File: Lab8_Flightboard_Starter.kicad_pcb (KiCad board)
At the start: 2 copper layers, 80 x 80 mm, 64 parts, among them J1 Motor1, J10 ESC3_GND, J11 ESC4_VBAT, J12 ESC4_GND, J2 Motor2, J3 Motor3, J4 Motor4, J5 ESC1_VBAT, J6 ESC1_GND, J7 ESC2_VBAT, J8 ESC2_GND, J9 ESC3_VBAT, Q1 DMP6023LE-13, U1 Teensy4.0, U2 TPS62933, U4 LP5912-3.3DRV, U5 LP5912-3.3DRV, U6 NRF24L01_Breakout, U9 LSM6DSO32_Adafruit

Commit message: Added hole positions
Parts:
- moved H2 115.5 mm to (214.0, 73.5)
- moved H4 114.9 mm to (214.0, 98.5)
- moved H3 90.2 mm to (189.0, 98.5)
- moved H1 90.2 mm to (189.0, 73.5)
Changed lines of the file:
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@@
 	(footprint "FC_Mechanical:MountingHole_3.3mm_no-courtyard"
 		(layer "F.Cu")
-		(at 99.13 85.95)
+		(at 214 73.5)
 		(descr "Mounting Hole 3.3mm, no annular, no courtyard")
 		(tags "mounting hole 3.3mm no annular, no courtyard")
@@
 	(footprint "FC_Mechanical:MountingHole_3.3mm_no-courtyard"
 		(layer "F.Cu")
-		(at 99.13 94.55)
+		(at 214 98.5)
 		(descr "Mounting Hole 3.3mm, no annular, no courtyard")
 		(tags "mounting hole 3.3mm no annular, no courtyard")
@@
 	(footprint "FC_Mechanical:MountingHole_3.3mm_no-courtyard"
 		(layer "F.Cu")
-		(at 99.13 81.65)
+		(at 189 73.5)
 		(descr "Mounting Hole 3.3mm, no annular, no courtyard")
 		(tags "mounting hole 3.3mm no annular, no courtyard")
@@
 	(footprint "FC_Mechanical:MountingHole_3.3mm_no-courtyard"
 		(layer "F.Cu")
-		(at 99.13 90.25)
+		(at 189 98.5)
 		(descr "Mounting Hole 3.3mm, no annular, no courtyard")
 		(tags "mounting hole 3.3mm no annular, no courtyard")

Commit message: Added key component locations
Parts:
- moved J7 159.9 mm to (230.1, 50.6)
- moved J8 159.9 mm to (237.4, 50.6)
- moved U6 143.4 mm to (231.7, 91.4)
- moved J11 142.1 mm to (230.2, 122.0)
- moved J12 142.1 mm to (237.5, 122.0)
- moved U9 137.5 mm to (201.5, 60.6)
- moved U1 122.4 mm to (200.9, 95.4), turned to 90 degrees
- moved J5 108.4 mm to (173.0, 50.1), turned to 180 degrees
- moved J6 97.5 mm to (165.7, 50.1), turned to 180 degrees
- moved J9 84.6 mm to (173.1, 121.3), turned to 180 degrees
- moved BT1 75.8 mm to (166.5, 88.0), turned to -90 degrees
- moved J10 70.2 mm to (165.8, 121.3), turned to 180 degrees
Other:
- board size 80 x 80 mm -> 80.5 x 80.5 mm

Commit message: Added motor through holes
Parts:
- moved J2 172.3 mm to (223.0, 64.5), turned to 90 degrees
- moved J4 150.1 mm to (223.0, 110.0), turned to 90 degrees
- moved J1 139.0 mm to (181.0, 64.5), turned to -90 degrees
- moved J3 113.3 mm to (181.0, 110.0), turned to -90 degrees
- moved U6 7.11 mm to (233.0, 84.4)
- moved U1 0.74 mm to (201.6, 95.4)
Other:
- board size 80.5 x 80.5 mm -> 80 x 80 mm

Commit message: Edited F Silkscreen text
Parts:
- Teensy 4.0: renamed from U1
- moved L1 101.5 mm to (178.5, 102.0), turned to 180 degrees
- moved C6 70.0 mm to (171.5, 107.5), turned to 90 degrees
- moved D2 67.0 mm to (178.5, 95.0), turned to 180 degrees
- renumbered U9 to LSM, J1 to M1, J2 to M2, J3 to M3, J4 to M4, U6 to NRF
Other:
- board text added: "J10"
- board text added: "J11"
- board text added: "J12"
- board text added: "J7"
- board text added: "J8"
- board text added: "J9"

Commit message: Placed down more components
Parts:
- moved Q1 112.4 mm to (177.5, 79.0)
- moved D1 73.8 mm to (186.0, 88.0)
- moved C2 69.4 mm to (172.5, 97.5), turned to -90 degrees
- moved C6 4.24 mm to (174.5, 104.5)
- moved D2 3.50 mm to (182.0, 95.0)
- moved L1 3.00 mm to (181.5, 102.0)
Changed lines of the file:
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@@
 			(at 0 1.85 0)
 			(layer "F.Fab")
+			(hide yes)
 			(effects
 				(font
@@
 	(footprint "Capacitor_SMD:C_1206_3216Metric_Pad1.33x1.80mm_HandSolder"
 		(layer "F.Cu")
-		(at 104.285 84.525)
+		(at 172.5 97.5 -90)
 		(descr "Capacitor SMD 1206 (3216 Metric), square (rectangular) end terminal, IPC-7351 nominal with elongated pad for handsoldering. (Body size source: IPC-SM-782 page 76, https://www.pcb-3d.com/wordpress/wp-content/uploads/ipc-sm-782a_amendment_1_and_2.pdf)")
 		(tags "capacitor handsolder")
 		(property "Reference" "C2"
-			(at 0 -1.85 0)
+			(at 0 -1.85 90)
 			(layer "F.SilkS")
 			(effects
@@
 		)
 		(property "Value" "10u"
-			(at 0 1.85 0)
+			(at 0 1.85 90)
 			(layer "F.Fab")
+			(hide yes)
 			(effects
 				(font
@@
 		)
 		(property "Datasheet" ""
-			(at 0 0 0)
+			(at 0 0 90)
 			(layer "F.Fab")
 			(hide yes)
@@
 		)
 		(property "Description" "Unpolarized capacitor, small symbol"
-			(at 0 0 0)
+			(at 0 0 90)
 			(layer "F.Fab")
 			(hide yes)
@@
 		)
 		(property "KiLib_Generator" "SMD_2terminal_chip_molded"
-			(at 0 0 0)
+			(at 0 0 90)
 			(layer "F.SilkS")
 			(hide yes)
@@
 		(duplicate_pad_numbers_are_jumpers no)
 		(fp_line
-			(start -0.711252 -0.91)
-			(end 0.711252 -0.91)
+			(start -0.711252 0.91)
+			(end 0.711252 0.91)
 			(stroke
 				(width 0.12)
@@
 		)
 		(fp_line
-			(start -0.711252 0.91)
-			(end 0.711252 0.91)
+			(start -0.711252 -0.91)
+			(end 0.711252 -0.91)
 			(stroke
 				(width 0.12)
@@
 			(layer "F.Fab")
 		)
-		(fp_text user "${REFERENCE}"
-			(at 0 0 0)
-			(layer "F.Fab")
-			(effects
-				(font
-					(size 0.8 0.8)
-					(thickness 0.12)
-				)
-			)
-		)
 		(pad "1" smd roundrect
-			(at -1.5625 0)
+			(at -1.5625 0 270)
 			(size 1.325 1.8)
 			(layers "F.Cu" "F.Mask" "F.Paste")
@@
 		)
 		(pad "2" smd roundrect
-			(at 1.5625 0)
+			(at 1.5625 0 270)
 			(size 1.325 1.8)
 			(layers "F.Cu" "F.Mask" "F.Paste")
@@
 	(footprint "FC_Power_Footprints:SMBJSeries_LTF"
 		(layer "F.Cu")
-		(at 112.4382 82.2987)
+		(at 186 88)
 		(tags "SMBJ17A ")
 		(property "Reference" "D1"
-			(at 0 0 0)
+			(at 0 -2.7987 0)
 			(unlocked yes)
 			(layer "F.SilkS")
@@
 			(unlocked yes)
 			(layer "F.Fab")
+			(hide yes)
 			(effects
 				(font
@@
 			(layer "F.Fab")
 		)
-		(fp_text user "${REFERENCE}"
-			(at 0 0 0)
-			(unlocked yes)
-			(layer "F.Fab")
-			(effects
-				(font
-					(size 1 1)
-					(thickness 0.15)
-				)
-			)
-		)
 		(pad "1" smd rect
 			(at -1.8542 0 90)
@@
 			(polygon
 				(pts
-					(xy 109.695 80.381) (xy 115.1814 80.381) (xy 115.1814 81.1557) (xy 109.695 81.1557)
+					(xy 183.2568 86.0823) (xy 188.7432 86.0823) (xy 188.7432 86.857) (xy 183.2568 86.857)
 				)
 			)
@@
 			(polygon
 				(pts
-					(xy 109.695 83.4417) (xy 115.1814 83.4417) (xy 115.1814 84.2164) (xy 109.695 84.2164)
+					(xy 183.2568 89.143) (xy 188.7432 89.143) (xy 188.7432 89.9177) (xy 183.2568 89.9177)
 				)
 			)
@@
 			(polygon
 				(pts
-					(xy 111.727 81.1557) (xy 113.1494 81.1557) (xy 113.1494 83.4417) (xy 111.727 83.4417)
+					(xy 185.2888 86.857) (xy 186.7112 86.857) (xy 186.7112 89.143) (xy 185.2888 89.143)
 				)
 			)
@@
 	(footprint "FC_Inductor_Footprints:IND_SRP7028A-4R7M_BRN"
 		(layer "F.Cu")
-		(at 178.5 102 180)
+		(at 181.5 102 180)
 		(tags "SRP7028A-4R7M ")
 		(property "Reference" "L1"
@@
 	(footprint "Capacitor_SMD:C_1206_3216Metric_Pad1.33x1.80mm_HandSolder"
 		(layer "F.Cu")
-		(at 171.5 107.5 90)
+		(at 174.5 104.5 90)
 		(descr "Capacitor SMD 1206 (3216 Metric), square (rectangular) end terminal, IPC-7351 nominal with elongated pad for handsoldering. (Body size source: IPC-SM-782 page 76, https://www.pcb-3d.com/wordpress/wp-content/uploads/ipc-sm-782a_amendment_1_and_2.pdf)")
 		(tags "capacitor handsolder")
@@
 	(footprint "FC_Power_Footprints:DMP6023LE-13_Official"
 		(layer "F.Cu")
-		(at 81.535 137.535)
+		(at 177.5 79)
 		(descr "DMP6023LE-13, SOT-223, official Diodes Incorporated suggested land pattern; https://www.diodes.com/assets/Package-Files/SOT223.pdf")
 		(tags "DMP6023LE-13 SOT-223 P-channel MOSFET")
@@
 			(at 0 5 0)
 			(layer "F.Fab")
+			(hide yes)
 			(effects
 				(font
@@
 	(footprint "FC_Diode_Footprints:DIOM5226X240N"
 		(layer "F.Cu")
-		(at 178.5 95 180)
+		(at 182 95 180)
 		(property "Reference" "D2"
 			(at 0 2.5 0)

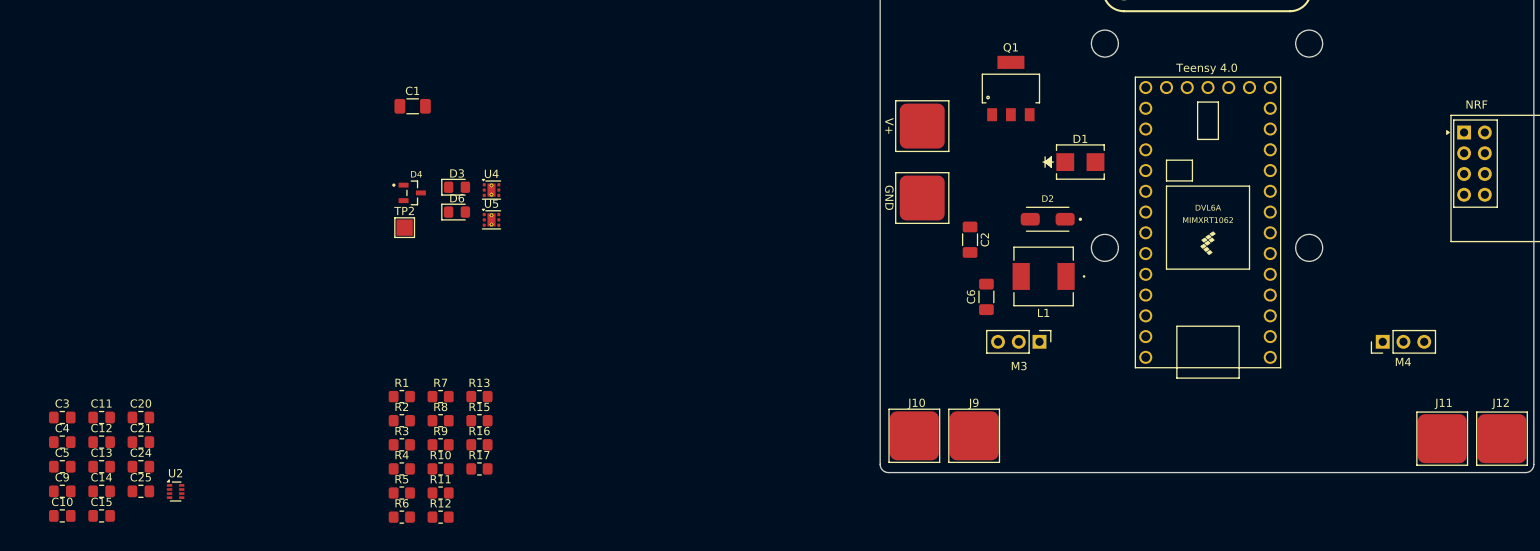
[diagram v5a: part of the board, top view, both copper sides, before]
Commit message: Added more components
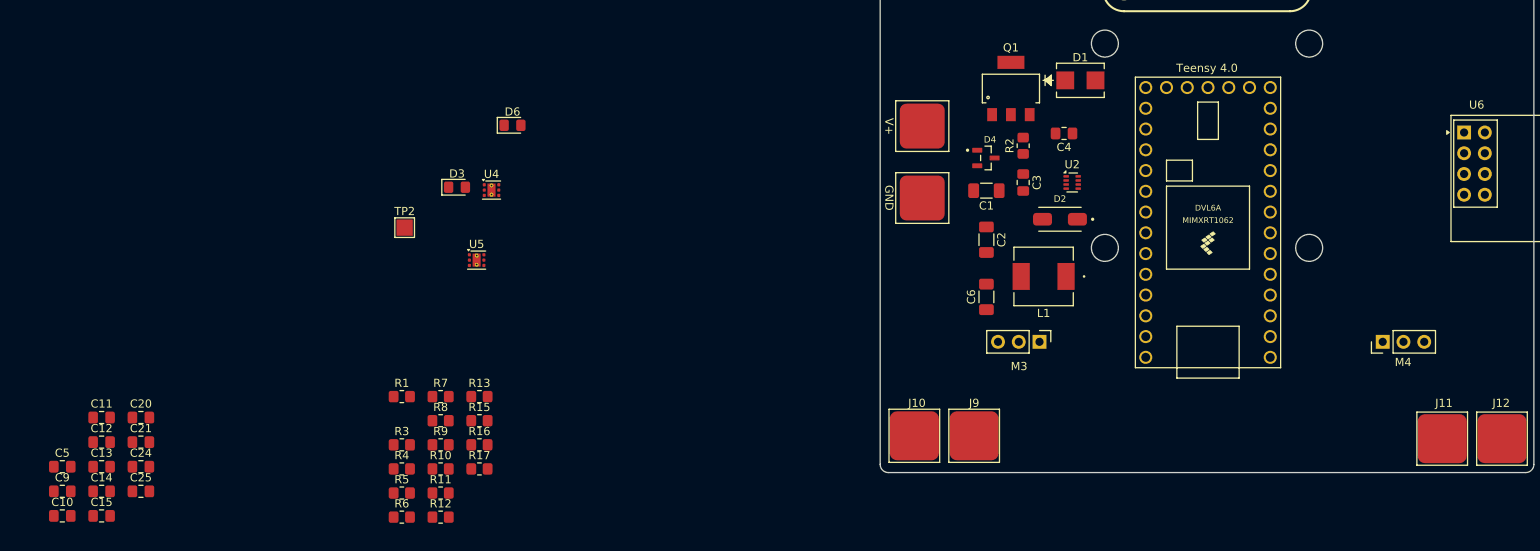
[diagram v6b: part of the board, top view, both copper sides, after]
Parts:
- moved C4 128.3 mm to (184.0, 84.5), turned to 180 degrees
- moved C3 121.1 mm to (179.0, 90.5), turned to -90 degrees
- moved U2 116.1 mm to (185.0, 90.5)
- moved R2 83.2 mm to (179.0, 86.0), turned to 90 degrees
- moved C1 71.0 mm to (174.5, 91.5), turned to 180 degrees
- moved D4 70.3 mm to (174.4, 87.5)
- moved D6 12.6 mm to (116.5, 83.5)
- moved D1 10.0 mm to (186.0, 78.0)
- moved U5 5.25 mm to (112.1, 100.0)
- moved C2 2.00 mm to (174.5, 97.5)
- moved D2 1.50 mm to (183.5, 95.0)
- renumbered NRF to U6

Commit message: Placed down all components
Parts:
- moved C21 116.7 mm to (183.2, 90.0), turned to 90 degrees
- moved C10 111.6 mm to (171.7, 114.0), turned to -90 degrees
- moved C20 111.5 mm to (178.7, 90.0), turned to 90 degrees
- moved C24 111.0 mm to (174.7, 85.6), turned to -90 degrees
- moved C25 108.6 mm to (170.2, 84.0), turned to 90 degrees
- moved C12 108.4 mm to (170.2, 91.6), turned to -90 degrees
- moved C9 104.0 mm to (164.2, 112.0), turned to -90 degrees
- moved C11 100.2 mm to (162.7, 92.0), turned to -90 degrees
- moved C5 77.2 mm to (135.2, 102.5), turned to -90 degrees
- moved C14 76.6 mm to (142.7, 132.5), turned to -90 degrees
- moved R8 75.8 mm to (171.7, 79.0), turned to 180 degrees
- moved R9 73.3 mm to (166.7, 79.0)
- moved C15 72.4 mm to (138.7, 132.5), turned to -90 degrees
- moved C13 69.0 mm to (135.2, 123.0), turned to 180 degrees
- moved TP2 68.9 mm to (172.2, 98.5)
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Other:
- board text removed: "J10"
- board text removed: "J11"
- board text removed: "J12"
- board text removed: "J7"
- board text removed: "J8"
- board text removed: "J9"

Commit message: Added some traces
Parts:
- moved R10 0.97 mm to (119.7, 121.5)
- moved R11 0.97 mm to (123.7, 121.5)
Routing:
- net /5V_OUT: track 0.00 -> 83.5 mm, vias 0 -> 5
- net /SYS_VIN: track 0.00 -> 32.5 mm
- net /M4_CMD: track 0.00 -> 29.2 mm
- net Net-(C6-Pad1): track 0.00 -> 19.9 mm
- net /M3_CMD: track 0.00 -> 18.0 mm
- net /VBAT_SENSE: track 0.00 -> 16.9 mm, vias 0 -> 4
- net /MOTOR4: track 0.00 -> 7.21 mm
- net Net-(U2-FB): track 0.00 -> 7.00 mm
- net Net-(U2-BST): track 0.00 -> 5.96 mm
- net Net-(U2-SW): track 0.00 -> 4.63 mm
- net Net-(U2-SS): track 0.00 -> 4.55 mm
- net /MOTOR3: track 0.00 -> 2.00 mm
- net GND: vias 0 -> 35
- added copper zone on F.Cu, net /VBAT
- added copper zone on B.Cu, net GND
